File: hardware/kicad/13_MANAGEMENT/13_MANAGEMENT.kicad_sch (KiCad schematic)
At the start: 13 parts

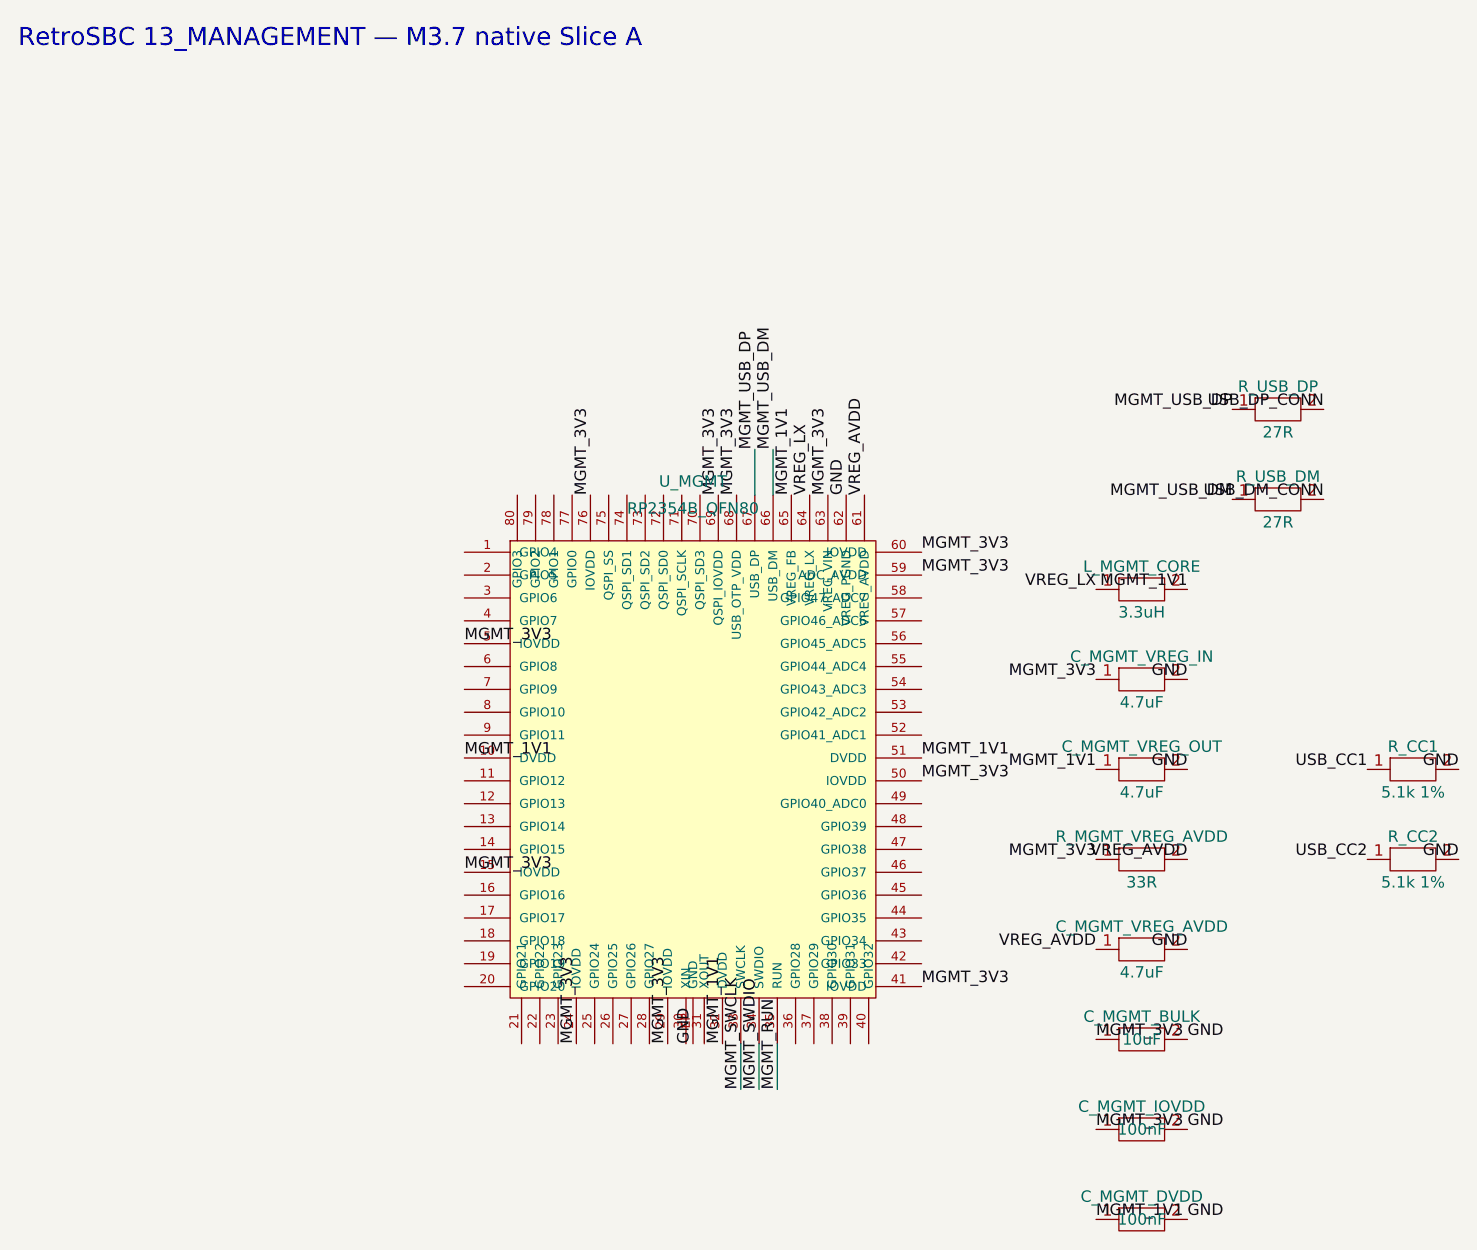
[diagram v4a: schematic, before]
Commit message: M3.7: remove dangling interface labels pending endpoints
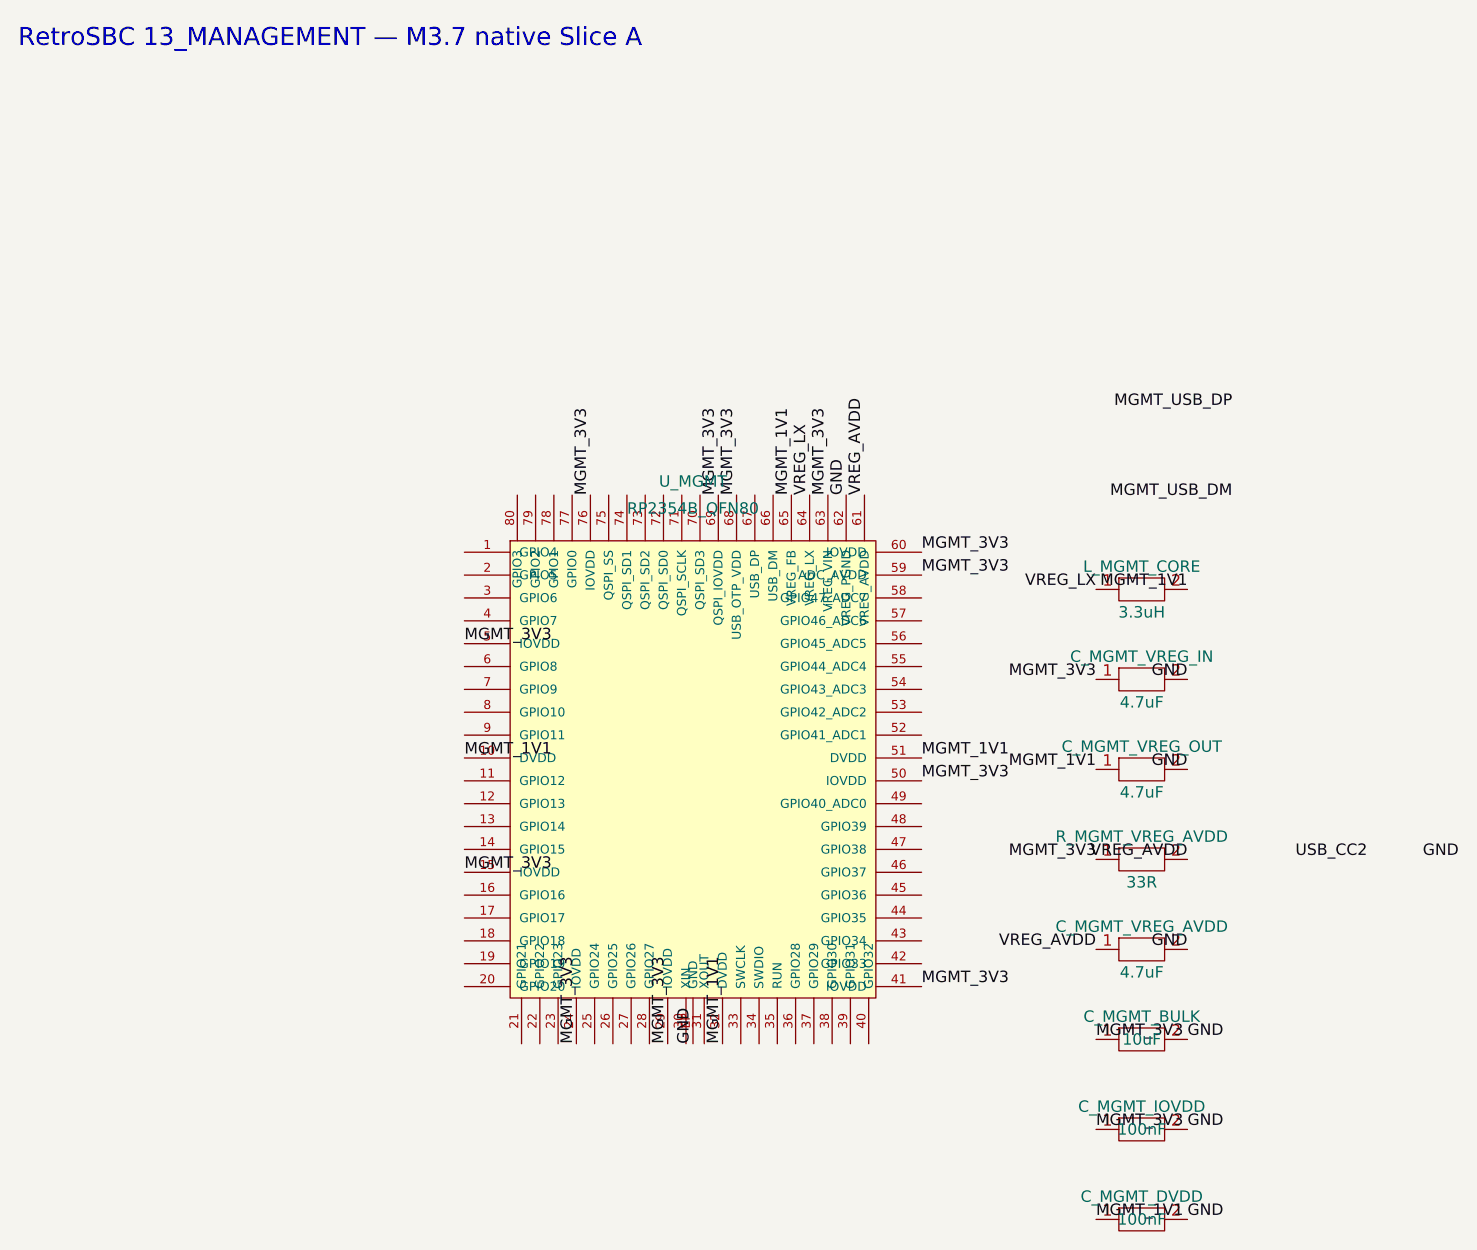
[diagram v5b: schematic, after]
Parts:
- removed R_CC1, R_CC2: 5.1k 1%, symbol RetroSBC-management:R_LOCAL
- removed R_USB_DM, R_USB_DP: 27R, symbol RetroSBC-management:R_LOCAL
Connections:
- net MGMT_USB_DM: no longer U_MGMT.66 (USB_DM)
- net MGMT_USB_DP: no longer U_MGMT.67 (USB_DP)
- net MGMT_RUN: no longer names the net of U_MGMT.35 (RUN)
- net MGMT_SWCLK: no longer names the net of U_MGMT.33 (SWCLK)
- net MGMT_SWDIO: no longer names the net of U_MGMT.34 (SWDIO)
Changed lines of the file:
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@@
     (effects (font (size 1.27 1.27)) (justify left bottom))
 )
-  (label "MGMT_SWCLK" (at 105.31 135.56 270)
-    (effects (font (size 1.27 1.27)) (justify left bottom))
-)
-  (label "MGMT_SWDIO" (at 107.34 135.56 270)
-    (effects (font (size 1.27 1.27)) (justify left bottom))
-)
-  (label "MGMT_RUN" (at 109.37 135.56 270)
-    (effects (font (size 1.27 1.27)) (justify left bottom))
-)
-  (label "MGMT_USB_DP" (at 106.87 64.44 90)
-    (effects (font (size 1.27 1.27)) (justify left bottom))
-)
-  (label "MGMT_USB_DM" (at 108.90 64.44 90)
-    (effects (font (size 1.27 1.27)) (justify left bottom))
-)
-  (wire (pts (xy 106.87 69.52) (xy 106.87 64.44)) (stroke (width 0) (type default)))
-  (wire (pts (xy 108.90 69.52) (xy 108.90 64.44)) (stroke (width 0) (type default)))
-  (wire (pts (xy 105.31 130.48) (xy 105.31 135.56)) (stroke (width 0) (type default)))
-  (wire (pts (xy 107.34 130.48) (xy 107.34 135.56)) (stroke (width 0) (type default)))
-  (wire (pts (xy 109.37 130.48) (xy 109.37 135.56)) (stroke (width 0) (type default)))
-  (symbol (lib_id "RetroSBC-management:R_LOCAL") (at 165 60 0) (unit 1)
-    (exclude_from_sim no) (in_bom yes) (on_board yes)
-    (property "Reference" "R_USB_DP" (at 165 57.46 0) (effects (font (size 1.27 1.27))))
-    (property "Value" "27R" (at 165 62.54 0) (effects (font (size 1.27 1.27))))
-    (property "Footprint" "" (at 165 60 0) (effects (font (size 1.27 1.27)) hide))
-    (property "Datasheet" "" (at 165 60 0) (effects (font (size 1.27 1.27)) hide))
-    (property "Description" "RP2354B USB series termination" (at 165 60 0) (effects (font (size 1.27 1.27)) hide))
-    (pin "1")
-    (pin "2")
-    (instances (project "RetroSBC-13-MANAGEMENT" (path "/7a5d3d51-9e2f-4d31-b7cb-9fbd10b8c301/71111111-1111-4111-8111-711111111111" (reference "R_USB_DP") (unit 1))))
-  )
   (label "MGMT_USB_DP" (at 159.92 60 0) (effects (font (size 1.27 1.27)) (justify right bottom)))
-  (label "USB_DP_CONN" (at 170.08 60 180) (effects (font (size 1.27 1.27)) (justify right bottom)))
-  (symbol (lib_id "RetroSBC-management:R_LOCAL") (at 165 70 0) (unit 1)
-    (exclude_from_sim no) (in_bom yes) (on_board yes)
-    (property "Reference" "R_USB_DM" (at 165 67.46 0) (effects (font (size 1.27 1.27))))
-    (property "Value" "27R" (at 165 72.54 0) (effects (font (size 1.27 1.27))))
-    (property "Footprint" "" (at 165 70 0) (effects (font (size 1.27 1.27)) hide))
-    (property "Datasheet" "" (at 165 70 0) (effects (font (size 1.27 1.27)) hide))
-    (property "Description" "RP2354B USB series termination" (at 165 70 0) (effects (font (size 1.27 1.27)) hide))
-    (pin "1")
-    (pin "2")
-    (instances (project "RetroSBC-13-MANAGEMENT" (path "/7a5d3d51-9e2f-4d31-b7cb-9fbd10b8c301/72111111-1111-4111-8111-722222222222" (reference "R_USB_DM") (unit 1))))
-  )
   (label "MGMT_USB_DM" (at 159.92 70 0) (effects (font (size 1.27 1.27)) (justify right bottom)))
-  (label "USB_DM_CONN" (at 170.08 70 180) (effects (font (size 1.27 1.27)) (justify right bottom)))
-  (symbol (lib_id "RetroSBC-management:R_LOCAL") (at 180 100 0) (unit 1)
-    (exclude_from_sim no) (in_bom yes) (on_board yes)
-    (property "Reference" "R_CC1" (at 180 97.46 0) (effects (font (size 1.27 1.27))))
-    (property "Value" "5.1k 1%" (at 180 102.54 0) (effects (font (size 1.27 1.27))))
-    (property "Footprint" "" (at 180 100 0) (effects (font (size 1.27 1.27)) hide))
-    (property "Datasheet" "" (at 180 100 0) (effects (font (size 1.27 1.27)) hide))
-    (property "Description" "USB-C UFP CC Rd" (at 180 100 0) (effects (font (size 1.27 1.27)) hide))
-    (pin "1")
-    (pin "2")
-    (instances (project "RetroSBC-13-MANAGEMENT" (path "/7a5d3d51-9e2f-4d31-b7cb-9fbd10b8c301/73111111-1111-4111-8111-733333333333" (reference "R_CC1") (unit 1))))
-  )
-  (label "USB_CC1" (at 174.92 100 0) (effects (font (size 1.27 1.27)) (justify right bottom)))
-  (label "GND" (at 185.08 100 180) (effects (font (size 1.27 1.27)) (justify right bottom)))
-  (symbol (lib_id "RetroSBC-management:R_LOCAL") (at 180 110 0) (unit 1)
-    (exclude_from_sim no) (in_bom yes) (on_board yes)
-    (property "Reference" "R_CC2" (at 180 107.46 0) (effects (font (size 1.27 1.27))))
-    (property "Value" "5.1k 1%" (at 180 112.54 0) (effects (font (size 1.27 1.27))))
-    (property "Footprint" "" (at 180 110 0) (effects (font (size 1.27 1.27)) hide))
-    (property "Datasheet" "" (at 180 110 0) (effects (font (size 1.27 1.27)) hide))
-    (property "Description" "USB-C UFP CC Rd" (at 180 110 0) (effects (font (size 1.27 1.27)) hide))
-    (pin "1")
-    (pin "2")
-    (instances (project "RetroSBC-13-MANAGEMENT" (path "/7a5d3d51-9e2f-4d31-b7cb-9fbd10b8c301/74111111-1111-4111-8111-744444444444" (reference "R_CC2") (unit 1))))
-  )
   (label "USB_CC2" (at 174.92 110 0) (effects (font (size 1.27 1.27)) (justify right bottom)))
   (label "GND" (at 185.08 110 180) (effects (font (size 1.27 1.27)) (justify right bottom)))

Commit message: M3.7: restore source-locked USB passive capture
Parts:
- added R_CC1, R_CC2: 5.1k 1%, symbol RetroSBC-management:R_LOCAL
- added R_USB_DM, R_USB_DP: 27R, symbol RetroSBC-management:R_LOCAL
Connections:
- net GND: now also R_CC2.2
- net MGMT_USB_DM: now also R_USB_DM.1
- net MGMT_USB_DP: now also R_USB_DP.1
- net USB_CC2: now also R_CC2.1
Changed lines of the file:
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@@
   (label "USB_CC2" (at 174.92 110 0) (effects (font (size 1.27 1.27)) (justify right bottom)))
   (label "GND" (at 185.08 110 180) (effects (font (size 1.27 1.27)) (justify right bottom)))
+  (symbol (lib_id "RetroSBC-management:R_LOCAL") (at 165 60 0) (unit 1)
+    (exclude_from_sim no) (in_bom yes) (on_board yes)
+    (property "Reference" "R_USB_DP" (at 165 57.46 0) (effects (font (size 1.27 1.27))))
+    (property "Value" "27R" (at 165 62.54 0) (effects (font (size 1.27 1.27))))
+    (property "Footprint" "" (at 165 60 0) (effects (font (size 1.27 1.27)) hide))
+    (property "Datasheet" "" (at 165 60 0) (effects (font (size 1.27 1.27)) hide))
+    (property "Description" "RP2354B USB series termination" (at 165 60 0) (effects (font (size 1.27 1.27)) hide))
+    (pin "1")
+    (pin "2")
+    (instances (project "RetroSBC-13-MANAGEMENT" (path "/7a5d3d51-9e2f-4d31-b7cb-9fbd10b8c301/71111111-1111-4111-8111-711111111111" (reference "R_USB_DP") (unit 1))))
+  )
+  (symbol (lib_id "RetroSBC-management:R_LOCAL") (at 165 70 0) (unit 1)
+    (exclude_from_sim no) (in_bom yes) (on_board yes)
+    (property "Reference" "R_USB_DM" (at 165 67.46 0) (effects (font (size 1.27 1.27))))
+    (property "Value" "27R" (at 165 72.54 0) (effects (font (size 1.27 1.27))))
+    (property "Footprint" "" (at 165 70 0) (effects (font (size 1.27 1.27)) hide))
+    (property "Datasheet" "" (at 165 70 0) (effects (font (size 1.27 1.27)) hide))
+    (property "Description" "RP2354B USB series termination" (at 165 70 0) (effects (font (size 1.27 1.27)) hide))
+    (pin "1")
+    (pin "2")
+    (instances (project "RetroSBC-13-MANAGEMENT" (path "/7a5d3d51-9e2f-4d31-b7cb-9fbd10b8c301/72111111-1111-4111-8111-722222222222" (reference "R_USB_DM") (unit 1))))
+  )
+  (symbol (lib_id "RetroSBC-management:R_LOCAL") (at 180 100 0) (unit 1)
+    (exclude_from_sim no) (in_bom yes) (on_board yes)
+    (property "Reference" "R_CC1" (at 180 97.46 0) (effects (font (size 1.27 1.27))))
+    (property "Value" "5.1k 1%" (at 180 102.54 0) (effects (font (size 1.27 1.27))))
+    (property "Footprint" "" (at 180 100 0) (effects (font (size 1.27 1.27)) hide))
+    (property "Datasheet" "" (at 180 100 0) (effects (font (size 1.27 1.27)) hide))
+    (property "Description" "USB-C UFP CC Rd" (at 180 100 0) (effects (font (size 1.27 1.27)) hide))
+    (pin "1")
+    (pin "2")
+    (instances (project "RetroSBC-13-MANAGEMENT" (path "/7a5d3d51-9e2f-4d31-b7cb-9fbd10b8c301/73111111-1111-4111-8111-733333333333" (reference "R_CC1") (unit 1))))
+  )
+  (symbol (lib_id "RetroSBC-management:R_LOCAL") (at 180 110 0) (unit 1)
+    (exclude_from_sim no) (in_bom yes) (on_board yes)
+    (property "Reference" "R_CC2" (at 180 107.46 0) (effects (font (size 1.27 1.27))))
+    (property "Value" "5.1k 1%" (at 180 112.54 0) (effects (font (size 1.27 1.27))))
+    (property "Footprint" "" (at 180 110 0) (effects (font (size 1.27 1.27)) hide))
+    (property "Datasheet" "" (at 180 110 0) (effects (font (size 1.27 1.27)) hide))
+    (property "Description" "USB-C UFP CC Rd" (at 180 110 0) (effects (font (size 1.27 1.27)) hide))
+    (pin "1")
+    (pin "2")
+    (instances (project "RetroSBC-13-MANAGEMENT" (path "/7a5d3d51-9e2f-4d31-b7cb-9fbd10b8c301/74111111-1111-4111-8111-744444444444" (reference "R_CC2") (unit 1))))
+  )
   (sheet_instances (path "/" (page "1")))
 )

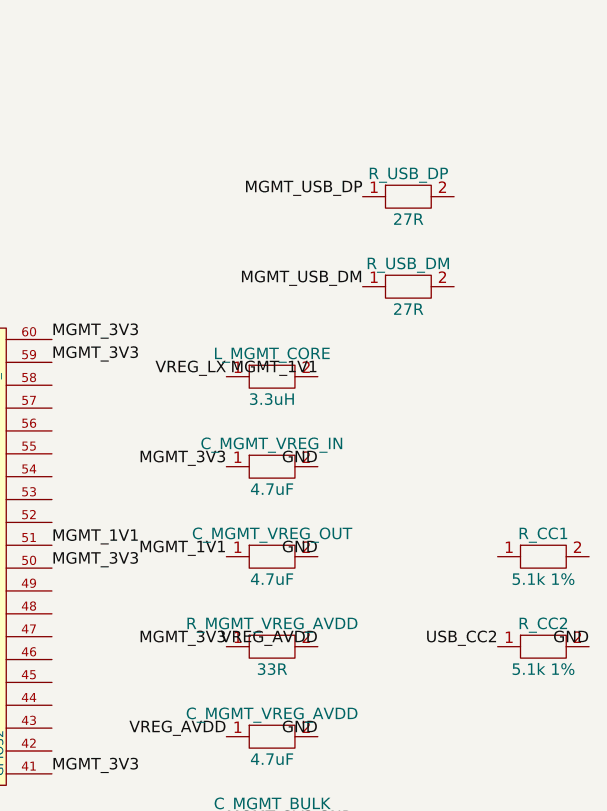
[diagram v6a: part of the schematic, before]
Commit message: M3.7: remove remaining dangling USB passive labels
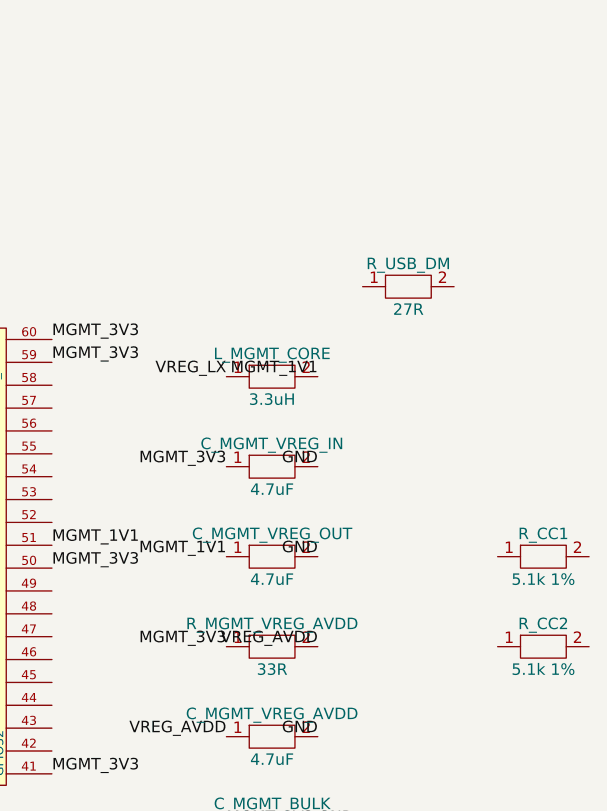
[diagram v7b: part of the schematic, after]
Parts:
- removed R_USB_DP: 27R, symbol RetroSBC-management:R_LOCAL
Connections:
- net GND: no longer R_CC2.2
- net MGMT_USB_DM: no longer names the net of R_USB_DM.1
- net USB_CC2: no longer names the net of R_CC2.1
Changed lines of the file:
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@@
     (effects (font (size 1.27 1.27)) (justify left bottom))
 )
-  (label "MGMT_USB_DP" (at 159.92 60 0) (effects (font (size 1.27 1.27)) (justify right bottom)))
-  (label "MGMT_USB_DM" (at 159.92 70 0) (effects (font (size 1.27 1.27)) (justify right bottom)))
-  (label "USB_CC2" (at 174.92 110 0) (effects (font (size 1.27 1.27)) (justify right bottom)))
-  (label "GND" (at 185.08 110 180) (effects (font (size 1.27 1.27)) (justify right bottom)))
-  (symbol (lib_id "RetroSBC-management:R_LOCAL") (at 165 60 0) (unit 1)
-    (exclude_from_sim no) (in_bom yes) (on_board yes)
-    (property "Reference" "R_USB_DP" (at 165 57.46 0) (effects (font (size 1.27 1.27))))
-    (property "Value" "27R" (at 165 62.54 0) (effects (font (size 1.27 1.27))))
-    (property "Footprint" "" (at 165 60 0) (effects (font (size 1.27 1.27)) hide))
-    (property "Datasheet" "" (at 165 60 0) (effects (font (size 1.27 1.27)) hide))
-    (property "Description" "RP2354B USB series termination" (at 165 60 0) (effects (font (size 1.27 1.27)) hide))
-    (pin "1")
-    (pin "2")
-    (instances (project "RetroSBC-13-MANAGEMENT" (path "/7a5d3d51-9e2f-4d31-b7cb-9fbd10b8c301/71111111-1111-4111-8111-711111111111" (reference "R_USB_DP") (unit 1))))
-  )
   (symbol (lib_id "RetroSBC-management:R_LOCAL") (at 165 70 0) (unit 1)
     (exclude_from_sim no) (in_bom yes) (on_board yes)

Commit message: M3.7: restore USB passives without interface labels
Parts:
- added R_USB_DP: 27R, symbol RetroSBC-management:R_LOCAL
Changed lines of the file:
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@@
     (instances (project "RetroSBC-13-MANAGEMENT" (path "/7a5d3d51-9e2f-4d31-b7cb-9fbd10b8c301/74111111-1111-4111-8111-744444444444" (reference "R_CC2") (unit 1))))
+  )
+  (symbol (lib_id "RetroSBC-management:R_LOCAL") (at 165 60 0) (unit 1)
+    (exclude_from_sim no) (in_bom yes) (on_board yes)
+    (property "Reference" "R_USB_DP" (at 165 57.46 0) (effects (font (size 1.27 1.27))))
+    (property "Value" "27R" (at 165 62.54 0) (effects (font (size 1.27 1.27))))
+    (property "Footprint" "" (at 165 60 0) (effects (font (size 1.27 1.27)) hide))
+    (property "Datasheet" "" (at 165 60 0) (effects (font (size 1.27 1.27)) hide))
+    (property "Description" "RP2354B USB series termination" (at 165 60 0) (effects (font (size 1.27 1.27)) hide))
+    (pin "1")
+    (pin "2")
+    (instances (project "RetroSBC-13-MANAGEMENT" (path "/7a5d3d51-9e2f-4d31-b7cb-9fbd10b8c301/71111111-1111-4111-8111-711111111111" (reference "R_USB_DP") (unit 1))))
   )
   (sheet_instances (path "/" (page "1")))
